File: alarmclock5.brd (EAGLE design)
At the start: 60 x 92 mm, 41 parts, among them X1 MKDSN1,5/2-5,08, X2 MKDSN1,5/2-5,08, X3 MKDSN1,5/2-5,08, X4 MKDSN1,5/2-5,08, X5 MKDSN1,5/2-5,08

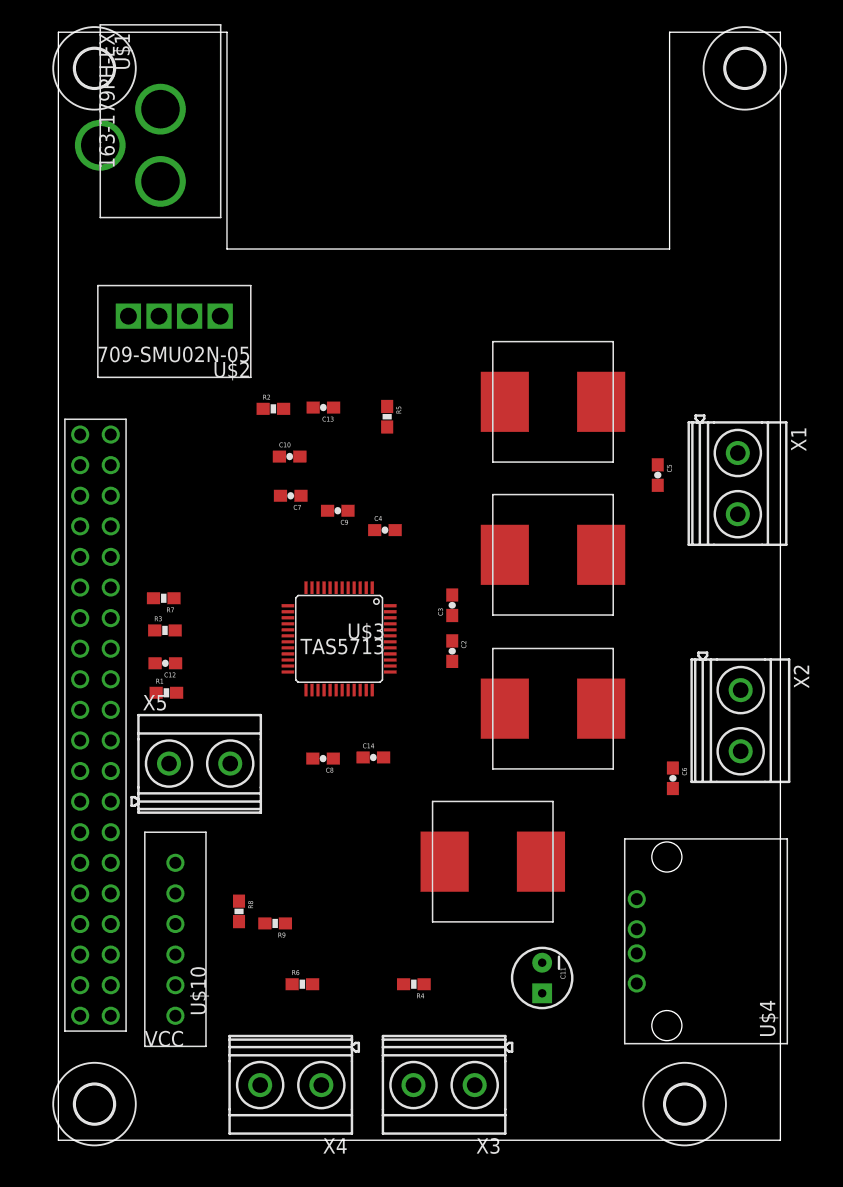
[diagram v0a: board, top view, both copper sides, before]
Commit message: fully routed
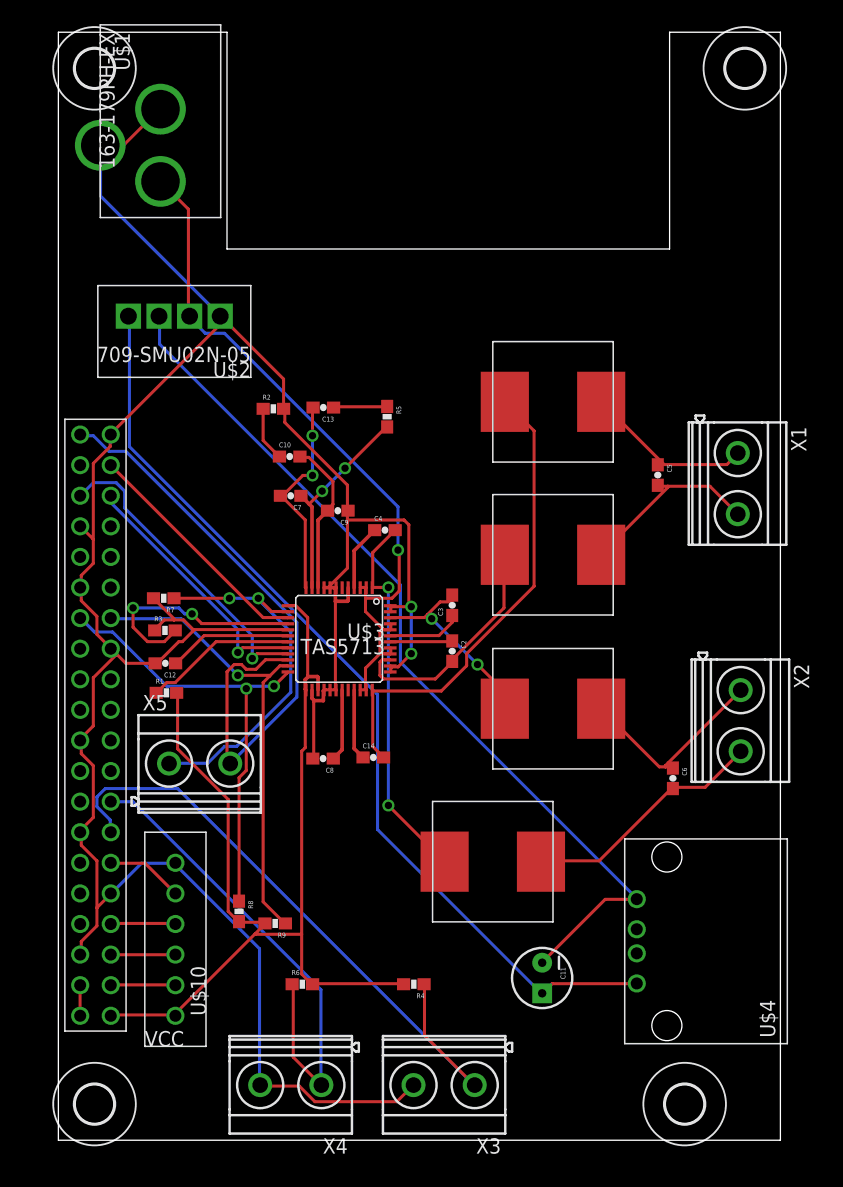
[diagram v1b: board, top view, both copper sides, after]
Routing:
- net GND: track 0.00 -> 224.0 mm, vias 0 -> 2
- net +3V3: track 0.00 -> 86.2 mm
- net N$3: track 0.00 -> 78.7 mm
- net N$29: track 0.00 -> 74.9 mm
- net VCC: track 0.00 -> 59.6 mm, vias 0 -> 1
- net N$8: track 0.00 -> 55.4 mm
- net N$1: track 0.00 -> 52.0 mm
- net N$6: track 0.00 -> 41.3 mm
- net N$10: track 0.00 -> 39.9 mm
- net N$35: track 0.00 -> 38.6 mm, vias 0 -> 1
- net N$36: track 0.00 -> 38.2 mm, vias 0 -> 2
- net N$13: track 0.00 -> 31.6 mm, vias 0 -> 2
- net N$34: track 0.00 -> 31.4 mm, vias 0 -> 2
- net N$5: track 0.00 -> 25.8 mm, vias 0 -> 1
- net N$4: track 0.00 -> 21.7 mm, vias 0 -> 1
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
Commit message: add a reset pin
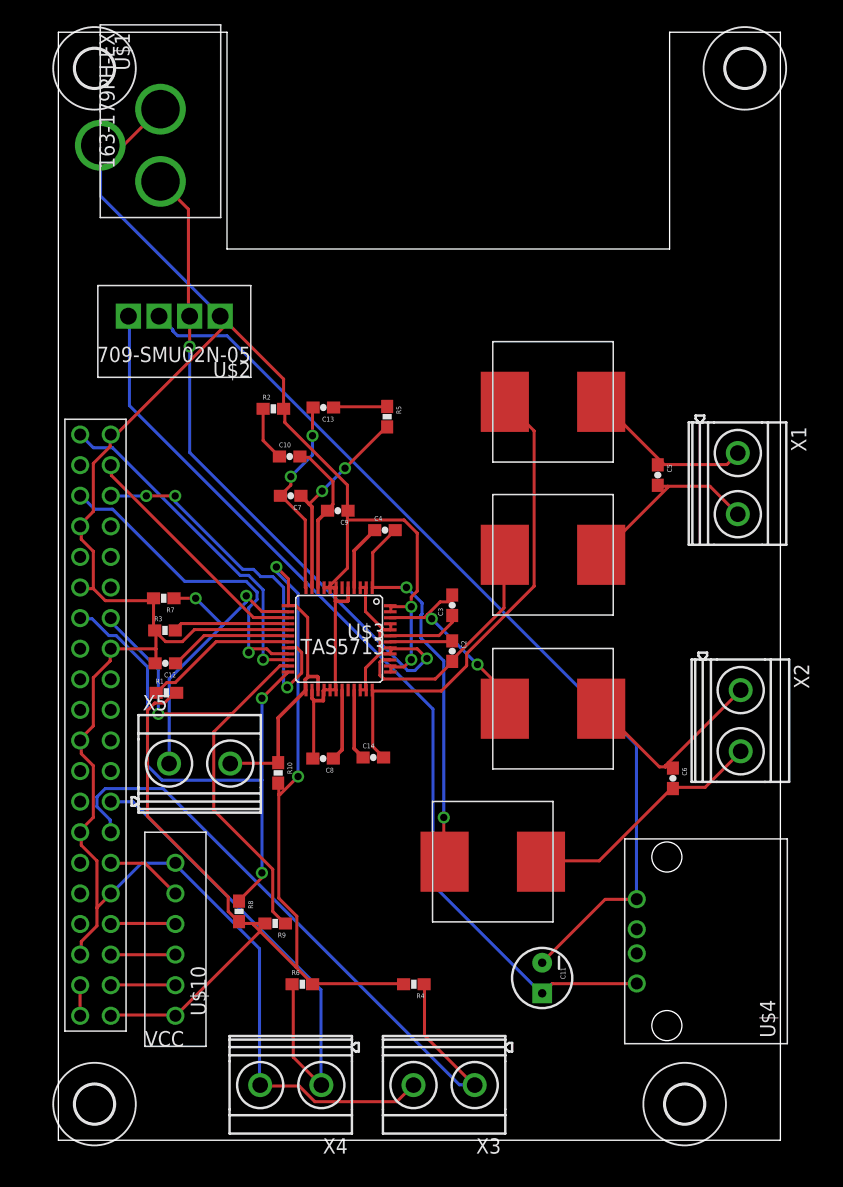
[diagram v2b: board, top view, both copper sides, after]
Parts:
- added R10: 10k, SparkFun-Passives:0603-RES
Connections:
- new net N$37: R10.1, U$3.P$25, X5.2
- net +3V3: now also R10.2; no longer U$3.P$25
- net N$1: no longer X5.2
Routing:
- net N$1: track 52.0 -> 28.4 mm, vias 0 -> 1
- net +3V3: track 86.2 -> 106.0 mm, vias 0 -> 2
- net N$37: track 0.00 -> 11.0 mm
- net N$7: track 19.4 -> 9.64 mm, vias 2 -> 0
- net N$4: track 21.7 -> 30.9 mm, vias 1 -> 3
- net VCC: track 59.6 -> 67.8 mm, vias 1 -> 2
- net N$36: track 38.2 -> 46.2 mm
- net N$34: track 31.4 -> 25.6 mm
- net N$35: track 38.6 -> 42.5 mm
- net N$29: track 74.9 -> 77.3 mm
- net GND: track 224.0 -> 222.6 mm
- net N$5: track 25.8 -> 26.8 mm
- net N$13: track 31.6 -> 32.5 mm
- net N$22: track 17.6 -> 17.0 mm

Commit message: bugfix: !reset! not connect directly to vcc
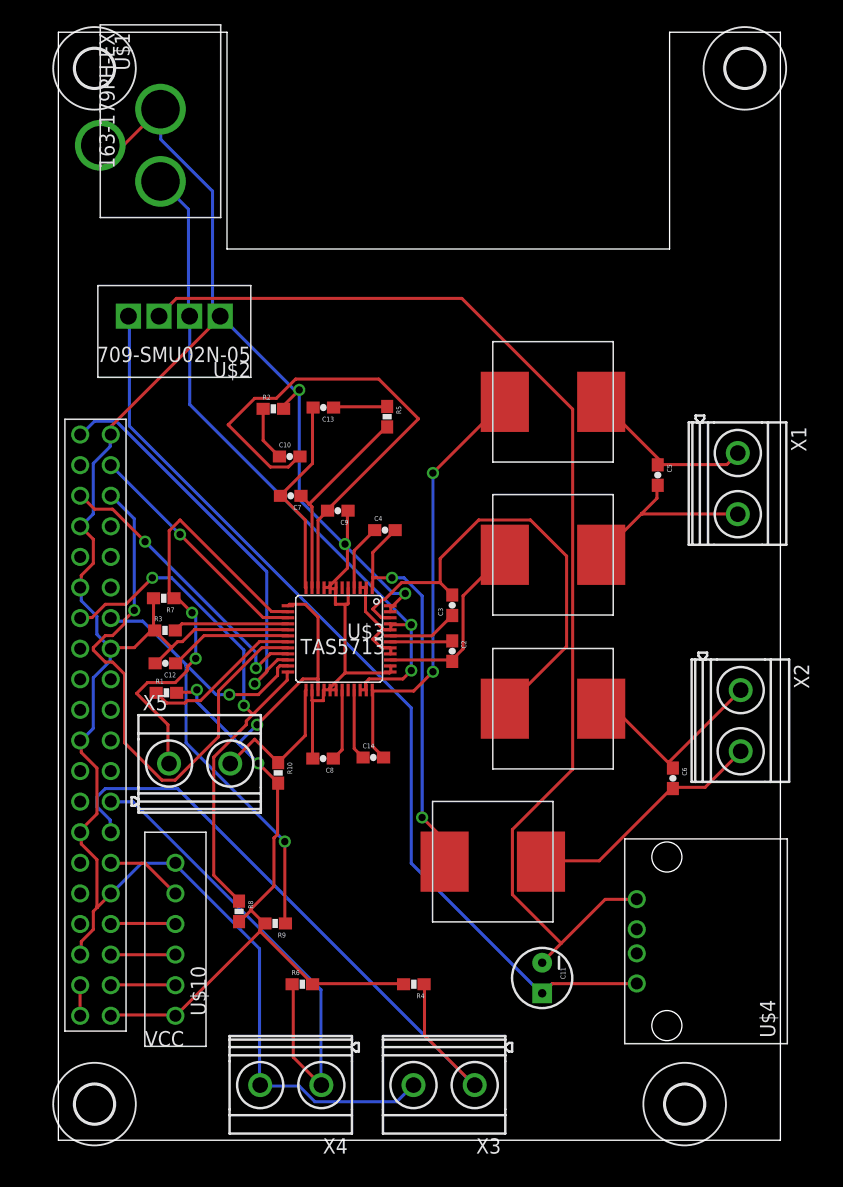
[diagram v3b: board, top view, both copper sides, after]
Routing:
- net +3V3: track 106.0 -> 74.8 mm, vias 2 -> 3
- net N$23: track 12.9 -> 44.0 mm
- net N$14: track 16.7 -> 39.6 mm, vias 2 -> 0
- net N$29: track 77.3 -> 96.9 mm
- net N$4: track 30.9 -> 46.2 mm, vias 3 -> 1
- net N$34: track 25.6 -> 38.4 mm
- net N$1: track 28.4 -> 34.5 mm
- net N$16: track 19.5 -> 15.9 mm
- net N$10: track 39.9 -> 36.6 mm, vias 0 -> 2
- net N$5: track 26.8 -> 24.4 mm, vias 1 -> 2
- net VCC: track 67.8 -> 65.6 mm
- net GND: track 222.6 -> 220.8 mm, vias 2 -> 3
- net N$37: track 11.0 -> 12.6 mm
- net N$13: track 32.5 -> 33.9 mm
- net N$35: track 42.5 -> 43.6 mm, vias 1 -> 2
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
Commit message: new board with RESET and PDN accessible via GPIO
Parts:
- removed X5: MKDSN1,5/2-5,08, con-phoenix-508:MKDSN1,5/2-5,08
- added C1: 0.1uF25V, SparkFun-Capacitors:0603-CAP
- added C15: 2200pF50V, SparkFun-Capacitors:0603-CAP
- moved C9 2.85 mm to (23.9, 55.0)
- moved C4 1.25 mm to (28.4, 50.7)
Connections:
- new net N$38: C1.1, U$3.P$32
- new net N$39: C15.1, U$3.P$6
- net GND: now also C1.2, C15.2
- net N$28: now also U$5.P$18
- net N$34: no longer X5.1
- net N$37: now also U$5.P$16; no longer X5.2
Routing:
- net N$10: track 36.6 -> 68.2 mm, vias 2 -> 0
- net N$23: track 44.0 -> 13.2 mm
- net N$34: track 38.4 -> 10.3 mm, vias 2 -> 0
- net N$4: track 46.2 -> 20.2 mm
- net N$29: track 96.9 -> 80.6 mm
- net N$13: track 33.9 -> 49.2 mm, vias 2 -> 0
- net N$37: track 12.6 -> 26.5 mm, vias 0 -> 3
- net N$27: track 10.3 -> 21.8 mm, vias 0 -> 4
- net N$38: track 0.00 -> 11.1 mm
- net N$28: track 13.4 -> 23.9 mm
- net N$22: track 17.0 -> 24.6 mm, vias 0 -> 2
- net N$8: track 55.4 -> 49.1 mm
- net GND: track 220.8 -> 226.4 mm, vias 3 -> 2
- net +3V3: track 74.8 -> 80.2 mm, vias 3 -> 2
- net N$35: track 43.6 -> 39.2 mm, vias 2 -> 1
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
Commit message: new schema
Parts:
- added C16: 330uF/25V, SparkFun-Passives:CPOL-RADIAL-10UF-25V
- added Q1: FDN360P, transistor-power:SUPER-SOT3
- added R11: 10k, SparkFun-Passives:0603-RES
- added T1: 2N2222, transistor:TO18
- moved U$2 2.70 mm to (6.11, 67.4)
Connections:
- new net N$40: T1.2, U$5.P$33
- new net N$41: Q1.1, R11.1, T1.3
- new net N$43: Q1.2, R11.2, U$1.VCC, U$2.VIN+
- net GND: now also C16.2, T1.1
- net VCC: now also C16.1, Q1.3; no longer U$1.VCC, U$2.VIN+
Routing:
- net GND: track 226.4 -> 288.6 mm, vias 2 -> 1
- net N$4: track 20.2 -> 74.6 mm, vias 1 -> 4
- net N$43: track 0.00 -> 32.1 mm, vias 0 -> 1
- net N$10: track 68.2 -> 39.9 mm
- net N$40: track 0.00 -> 22.5 mm, vias 0 -> 2
- net N$16: track 18.2 -> 39.9 mm
- net N$14: track 36.6 -> 17.5 mm, vias 0 -> 2
- net N$13: track 49.2 -> 32.2 mm, vias 0 -> 2
- net VCC: track 65.8 -> 51.2 mm, vias 2 -> 0
- net N$27: track 21.8 -> 10.3 mm, vias 4 -> 0
- net N$8: track 49.1 -> 59.5 mm
- net N$41: track 0.00 -> 10.2 mm
- net N$22: track 24.6 -> 17.4 mm
- net N$3: track 78.7 -> 85.3 mm
- net +3V3: track 80.2 -> 76.6 mm, vias 2 -> 3
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
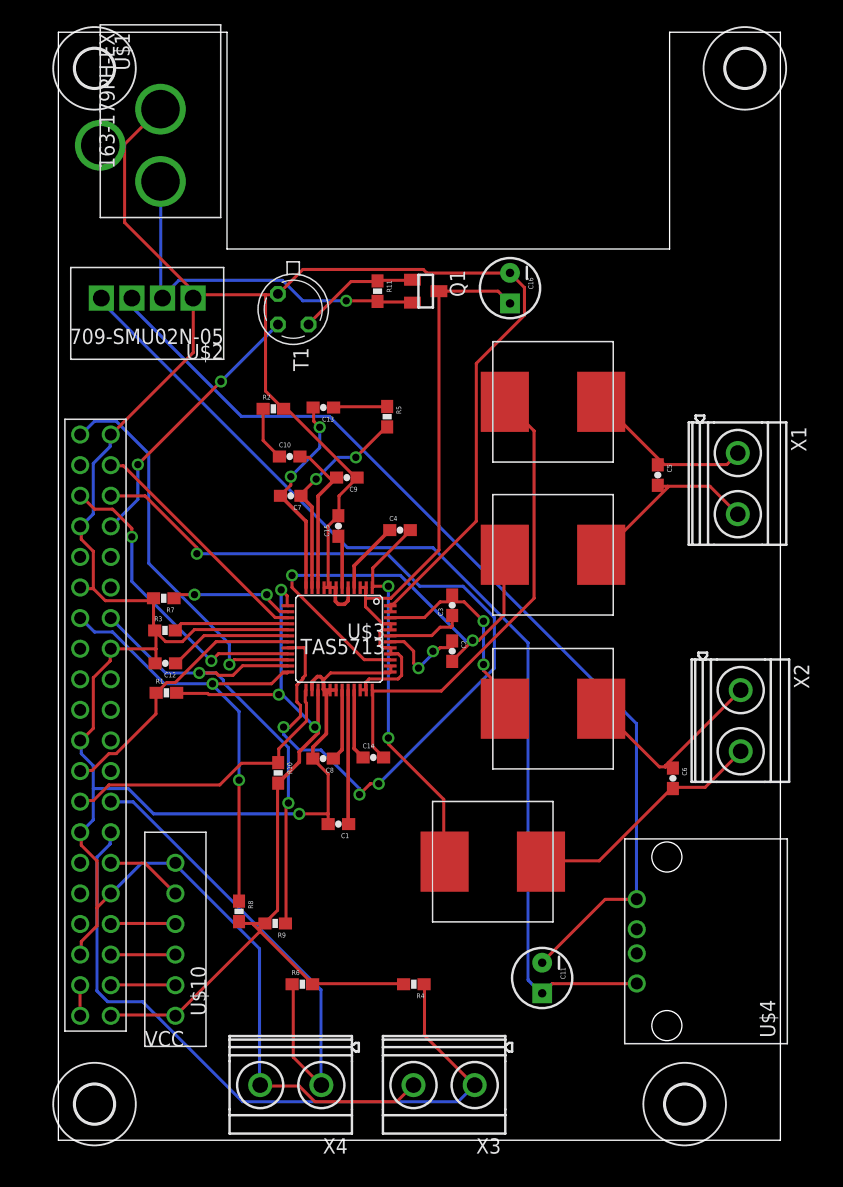
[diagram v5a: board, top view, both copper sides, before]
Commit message: add a R10k resistor to flush the capa
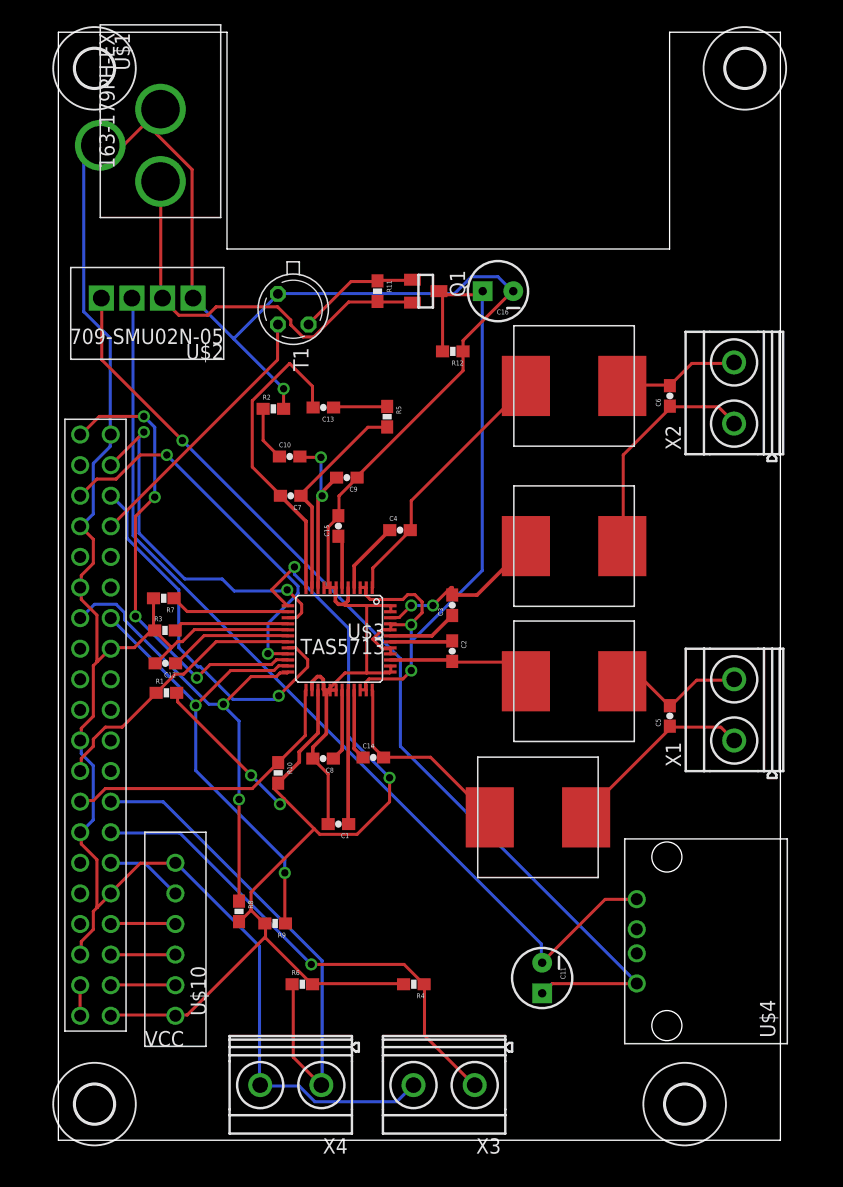
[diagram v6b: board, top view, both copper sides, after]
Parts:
- added R12: 10k, SparkFun-Passives:0603-RES
- moved U$9 40.1 mm to (42.8, 62.6)
- moved U$6 34.5 mm to (39.8, 26.8)
- moved C6 31.8 mm to (50.8, 61.8), turned to 90 degrees
- moved X2 27.3 mm to (56.1, 62.1), turned to 90 degrees
- moved C5 20.0 mm to (50.8, 35.2), turned to 90 degrees
- moved X1 18.8 mm to (56.1, 35.8), turned to 90 degrees
- moved U$8 13.6 mm to (42.8, 49.3)
- moved U$7 10.6 mm to (42.8, 38.1)
- moved C16 1.03 mm to (36.5, 70.5), turned to 180 degrees
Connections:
- net GND: now also R12.1
- net VCC: now also R12.2
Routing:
- net N$4: track 74.6 -> 31.2 mm, vias 4 -> 1
- net +3V3: track 76.6 -> 104.6 mm, vias 3 -> 4
- net N$16: track 39.9 -> 12.0 mm, vias 2 -> 0
- net N$10: track 39.9 -> 16.9 mm
- net GND: track 288.6 -> 270.3 mm
- net N$8: track 59.5 -> 41.4 mm, vias 0 -> 1
- net VCC: track 51.2 -> 64.8 mm, vias 0 -> 2
- net N$2: track 20.0 -> 30.5 mm, vias 0 -> 2
- net N$18: track 20.4 -> 10.2 mm
- net N$13: track 32.2 -> 22.1 mm, vias 2 -> 0
- net N$22: track 17.4 -> 26.2 mm, vias 2 -> 0
- net N$5: track 25.8 -> 32.3 mm
- net N$1: track 32.6 -> 38.9 mm, vias 1 -> 4
- net N$19: track 15.6 -> 11.8 mm
- net N$14: track 17.5 -> 14.6 mm
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
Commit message: update especially mouser.lbr
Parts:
- C16: value 330uF/25V -> 680uF/25V
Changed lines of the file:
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@@
 <element name="R11" library="SparkFun-Passives" package="0603-RES" value="10k" x="26.5" y="70.5" rot="R270"/>
 <element name="Q1" library="transistor-power" package="SUPER-SOT3" value="FDN360P" x="30.5" y="70.5" rot="R270"/>
-<element name="C16" library="SparkFun-Passives" package="CPOL-RADIAL-10UF-25V" value="330uF/25V" x="36.5" y="70.5" rot="R180"/>
+<element name="C16" library="SparkFun-Passives" package="CPOL-RADIAL-10UF-25V" value="680uF/25V" x="36.5" y="70.5" rot="R180"/>
 <element name="R12" library="SparkFun-Passives" package="0603-RES" value="10k" x="32.75" y="65.5" rot="R180"/>
 </elements>
